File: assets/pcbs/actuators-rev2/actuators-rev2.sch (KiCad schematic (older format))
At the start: 14 parts, among them J2 Screw_Terminal_01x02, J3 Screw_Terminal_01x02, J5 40HAT, J6 Conn_01x02, J7 Screw_Terminal_01x02, U1 ULN2003A, U2 PDQ15-Q24-S5-D

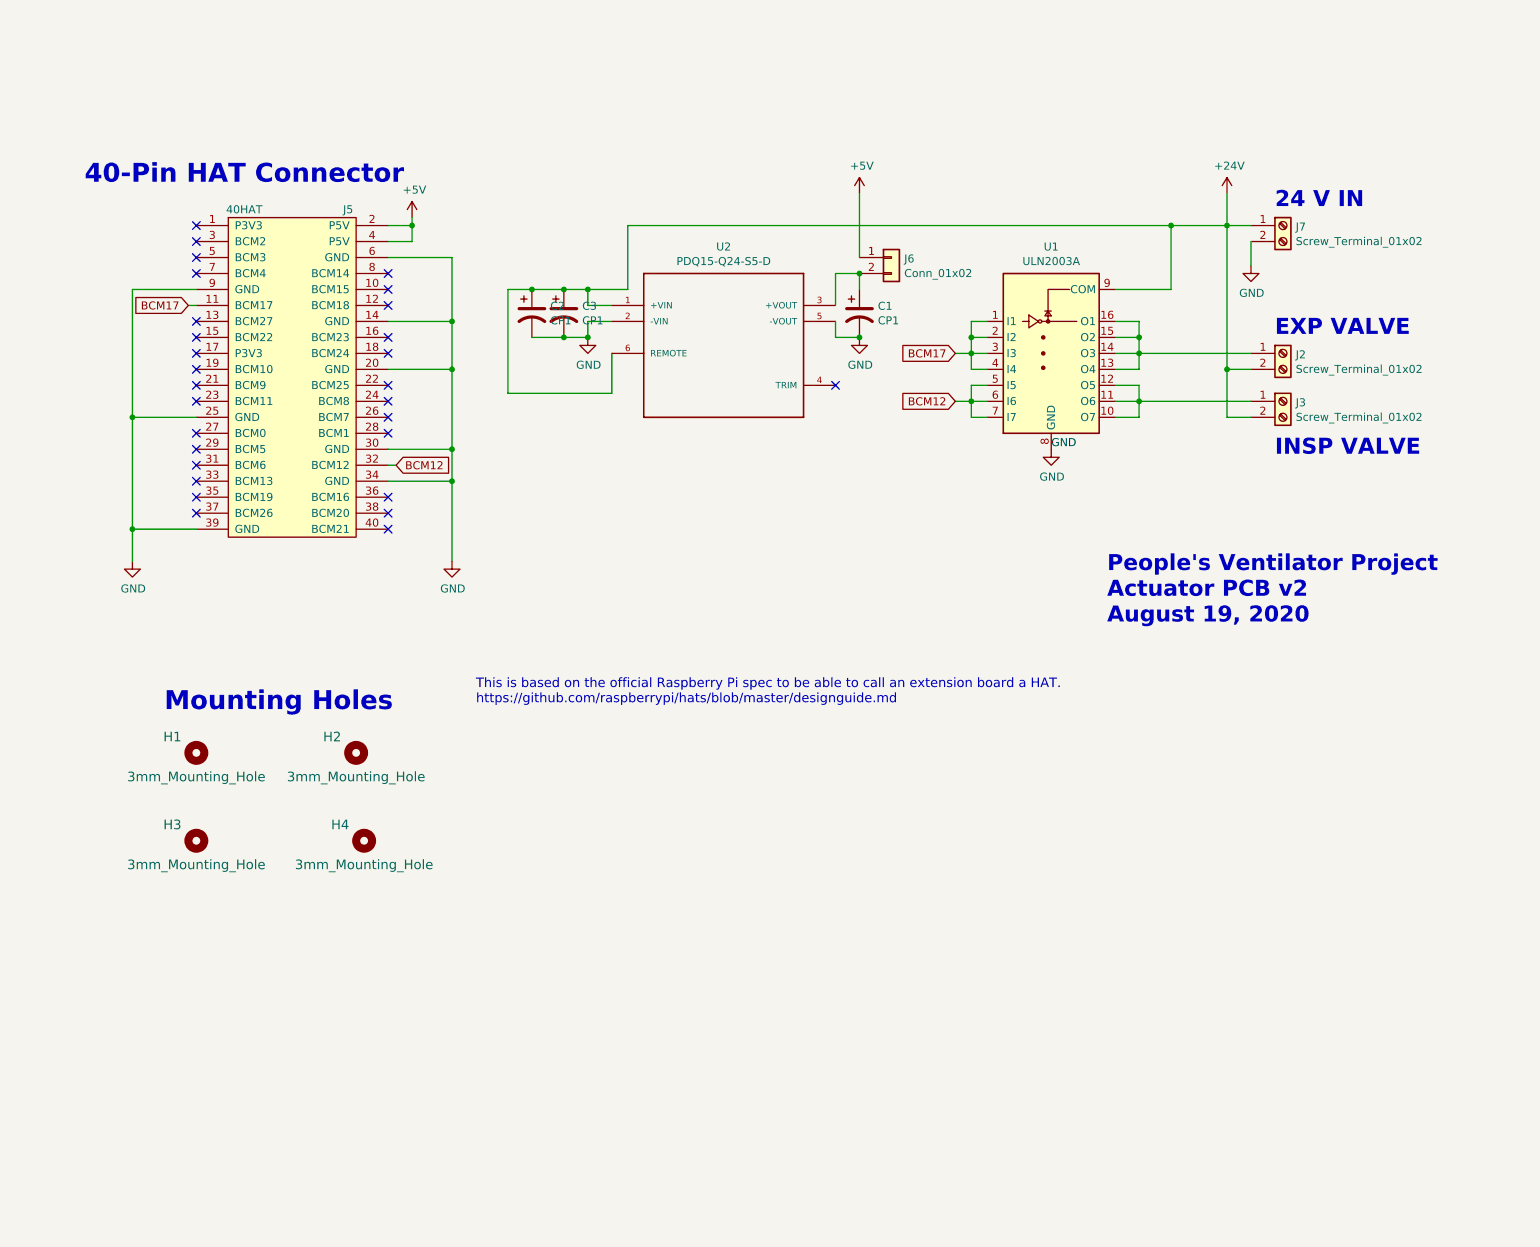
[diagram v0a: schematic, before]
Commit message: Added v1 of pcbs and revision history readme
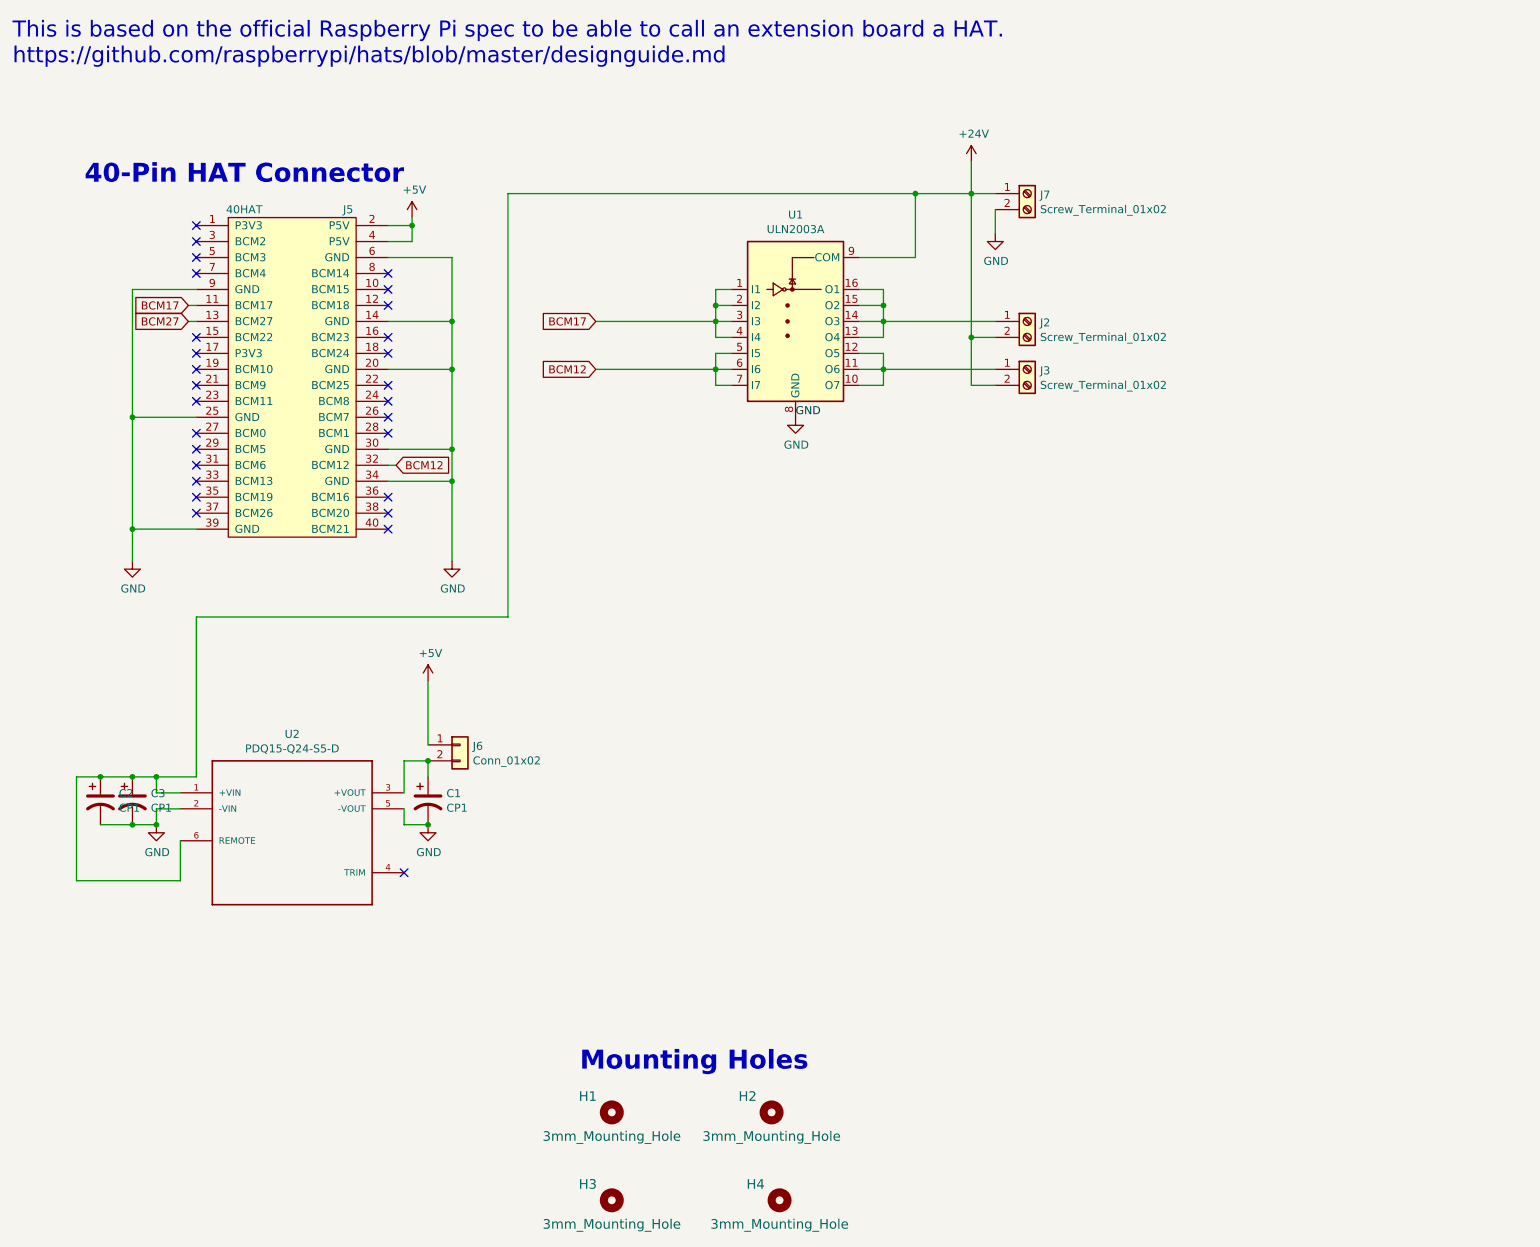
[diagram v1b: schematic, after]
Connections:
- net BCM27: now reaches J5.13 (BCM27)
- no-connect marks 29 -> 28
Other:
- note removed: "24 V IN"
- note removed: "EXP VALVE"
- note removed: "INSP VALVE"
- note removed: "People's Ventilator Project\nActuator PCB v2\nAugust 19, 2020"
- moved on the sheet: C1, C2, C3, H1, H2, H3, H4, J2, J3, J6, J7, U1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

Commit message: revised, added schematic images
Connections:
- net BCM27: no longer names the net of J5.13 (BCM27)
- no-connect marks 28 -> 29
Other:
- note added: "24 V IN"
- note added: "EXP VALVE"
- note added: "INSP VALVE"
- note added: "People's Ventilator Project\nActuator PCB v2\nAugust 19, 2020"
- moved on the sheet: C1, C2, C3, H1, H2, H3, H4, J2, J3, J6, J7, U1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
